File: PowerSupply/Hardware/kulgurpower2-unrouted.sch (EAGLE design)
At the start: 182 parts, among them M1 MST2V, M2 MST2V, M3 MST2V, M4 MST2V, Q1 BSH103, Q2 BSH103, Q3 BSH103, Q4 BSH103, X1 1727036, X2 2534-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

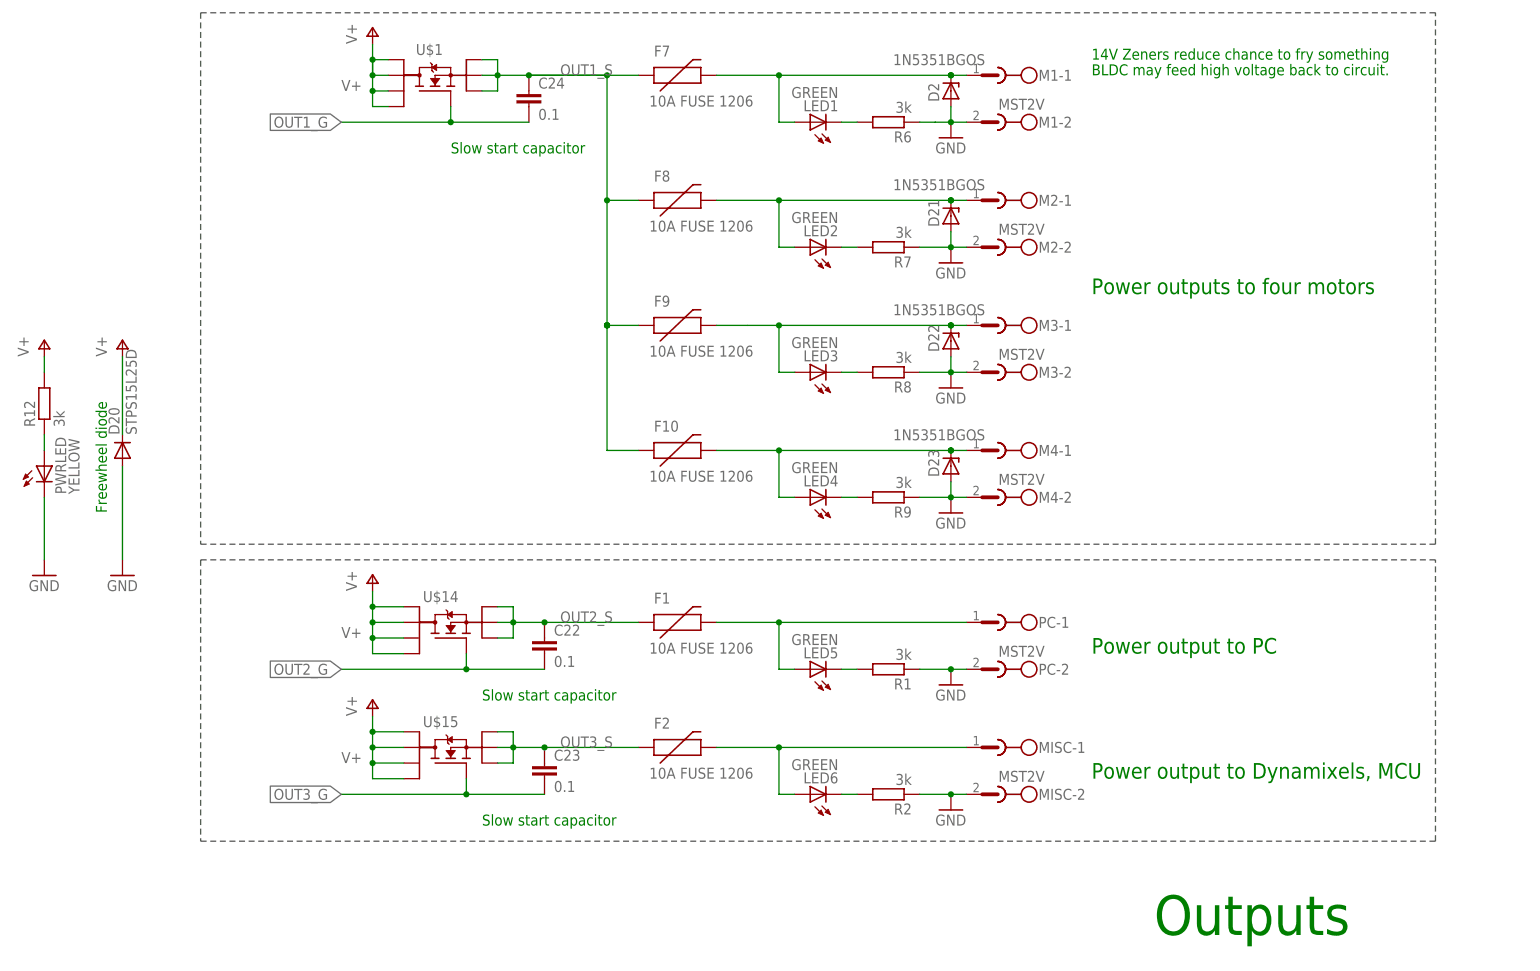
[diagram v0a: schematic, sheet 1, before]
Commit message: Schematic component type fixes
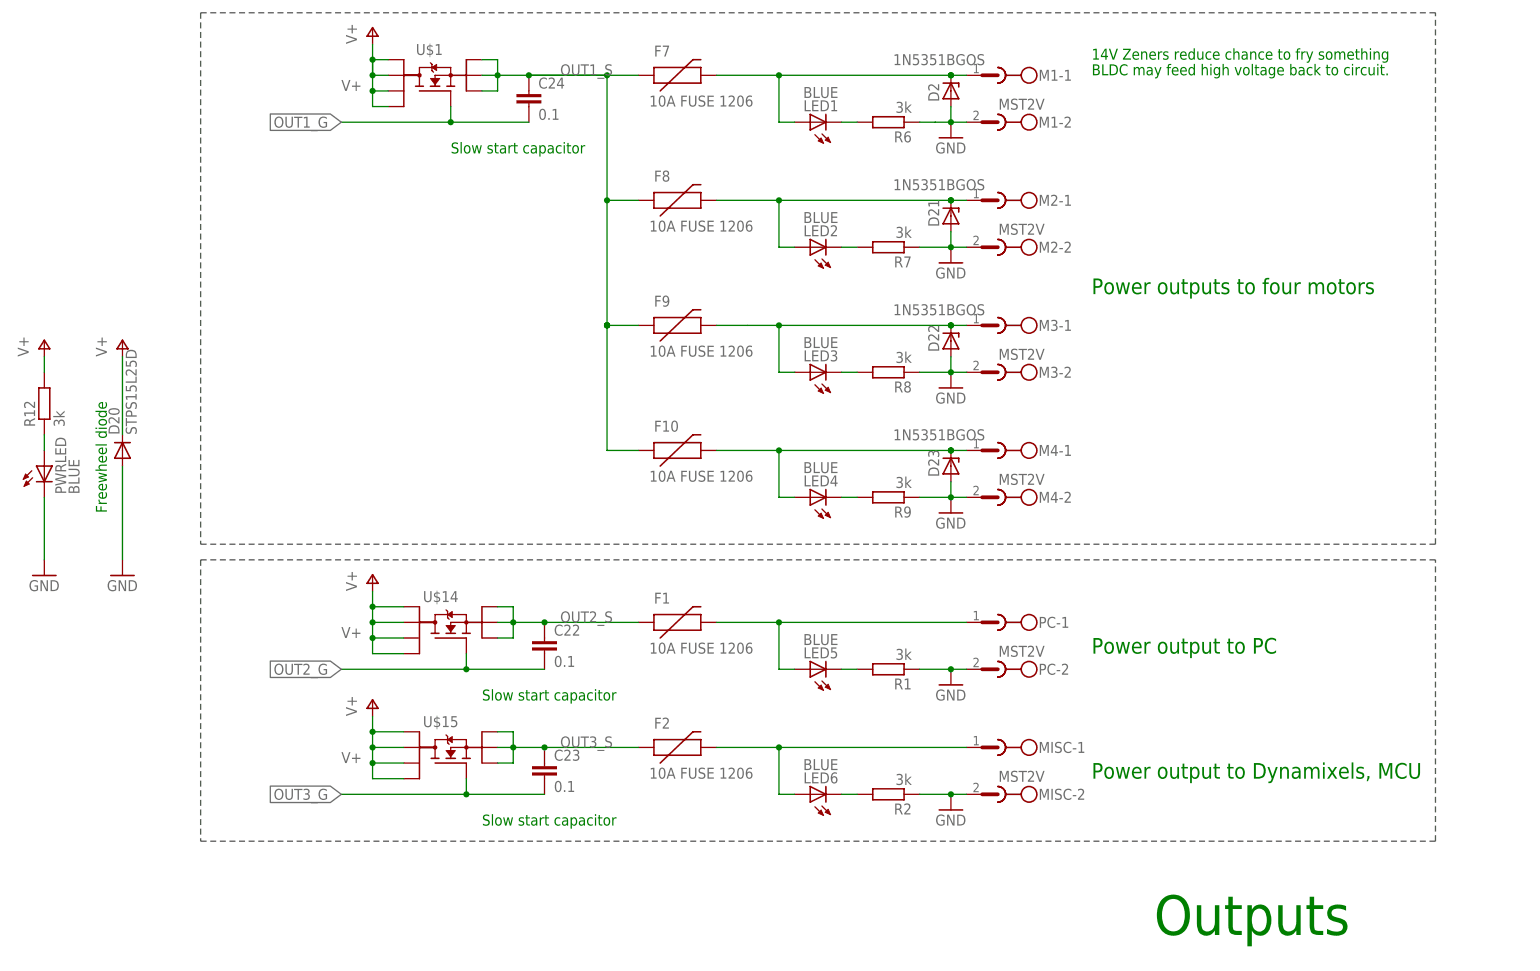
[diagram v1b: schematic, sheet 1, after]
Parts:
- LED1, LED2, LED3, LED4, LED5, LED6: value GREEN -> BLUE
- PWRLED: value YELLOW -> BLUE
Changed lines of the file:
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@@
 <part name="M4" library="con-phoenix-508" deviceset="MST2V" device=""/>
 <part name="P+2" library="supply1" deviceset="V+" device=""/>
-<part name="LED1" library="led" deviceset="LED" device="CHIP-LED0603" value="GREEN"/>
-<part name="LED2" library="led" deviceset="LED" device="CHIP-LED0603" value="GREEN"/>
-<part name="LED3" library="led" deviceset="LED" device="CHIP-LED0603" value="GREEN"/>
-<part name="LED4" library="led" deviceset="LED" device="CHIP-LED0603" value="GREEN"/>
-<part name="PWRLED" library="led" deviceset="LED" device="CHIP-LED0603" value="YELLOW"/>
+<part name="LED1" library="led" deviceset="LED" device="CHIP-LED0603" value="BLUE"/>
+<part name="LED2" library="led" deviceset="LED" device="CHIP-LED0603" value="BLUE"/>
+<part name="LED3" library="led" deviceset="LED" device="CHIP-LED0603" value="BLUE"/>
+<part name="LED4" library="led" deviceset="LED" device="CHIP-LED0603" value="BLUE"/>
+<part name="PWRLED" library="led" deviceset="LED" device="CHIP-LED0603" value="BLUE"/>
 <part name="R12" library="rcl" deviceset="R-EU_" device="R0603" value="3k"/>
 <part name="P+3" library="supply1" deviceset="V+" device=""/>
@@
 <part name="F1" library="SparkFun-PowerIC" deviceset="PTC" device="SMD" value="10A FUSE 1206"/>
 <part name="F2" library="SparkFun-PowerIC" deviceset="PTC" device="SMD" value="10A FUSE 1206"/>
-<part name="LED5" library="led" deviceset="LED" device="CHIP-LED0603" value="GREEN"/>
+<part name="LED5" library="led" deviceset="LED" device="CHIP-LED0603" value="BLUE"/>
 <part name="R1" library="rcl" deviceset="R-EU_" device="R0603" value="3k"/>
-<part name="LED6" library="led" deviceset="LED" device="CHIP-LED0603" value="GREEN"/>
+<part name="LED6" library="led" deviceset="LED" device="CHIP-LED0603" value="BLUE"/>
 <part name="R2" library="rcl" deviceset="R-EU_" device="R0603" value="3k"/>
 <part name="GND3" library="supply1" deviceset="GND" device=""/>

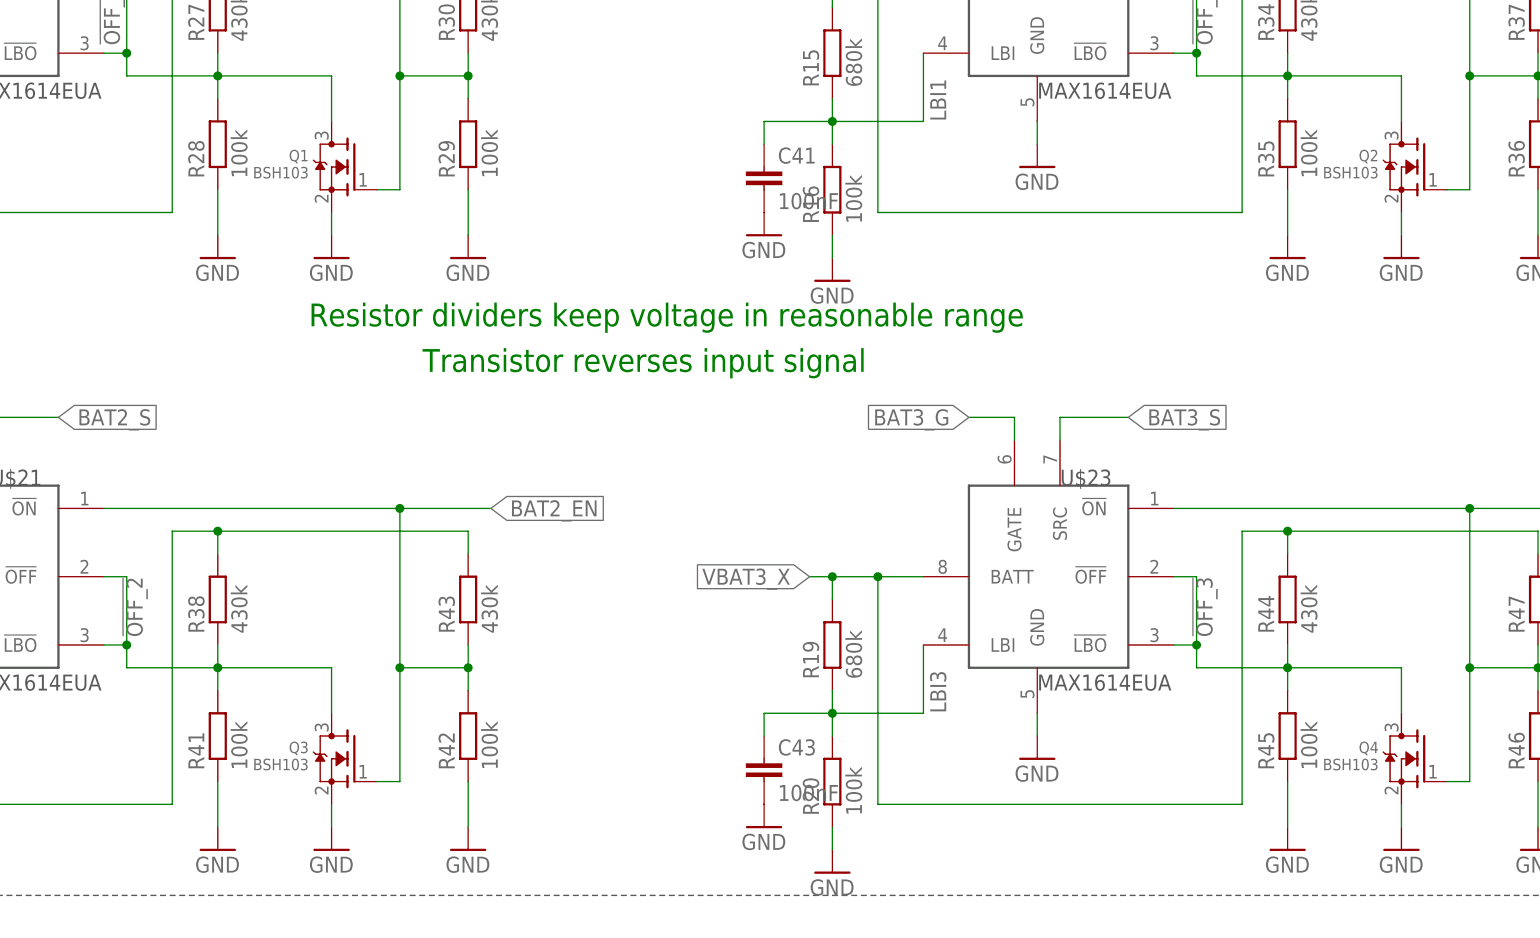
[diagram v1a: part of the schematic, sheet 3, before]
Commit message: Some values changed in schematic
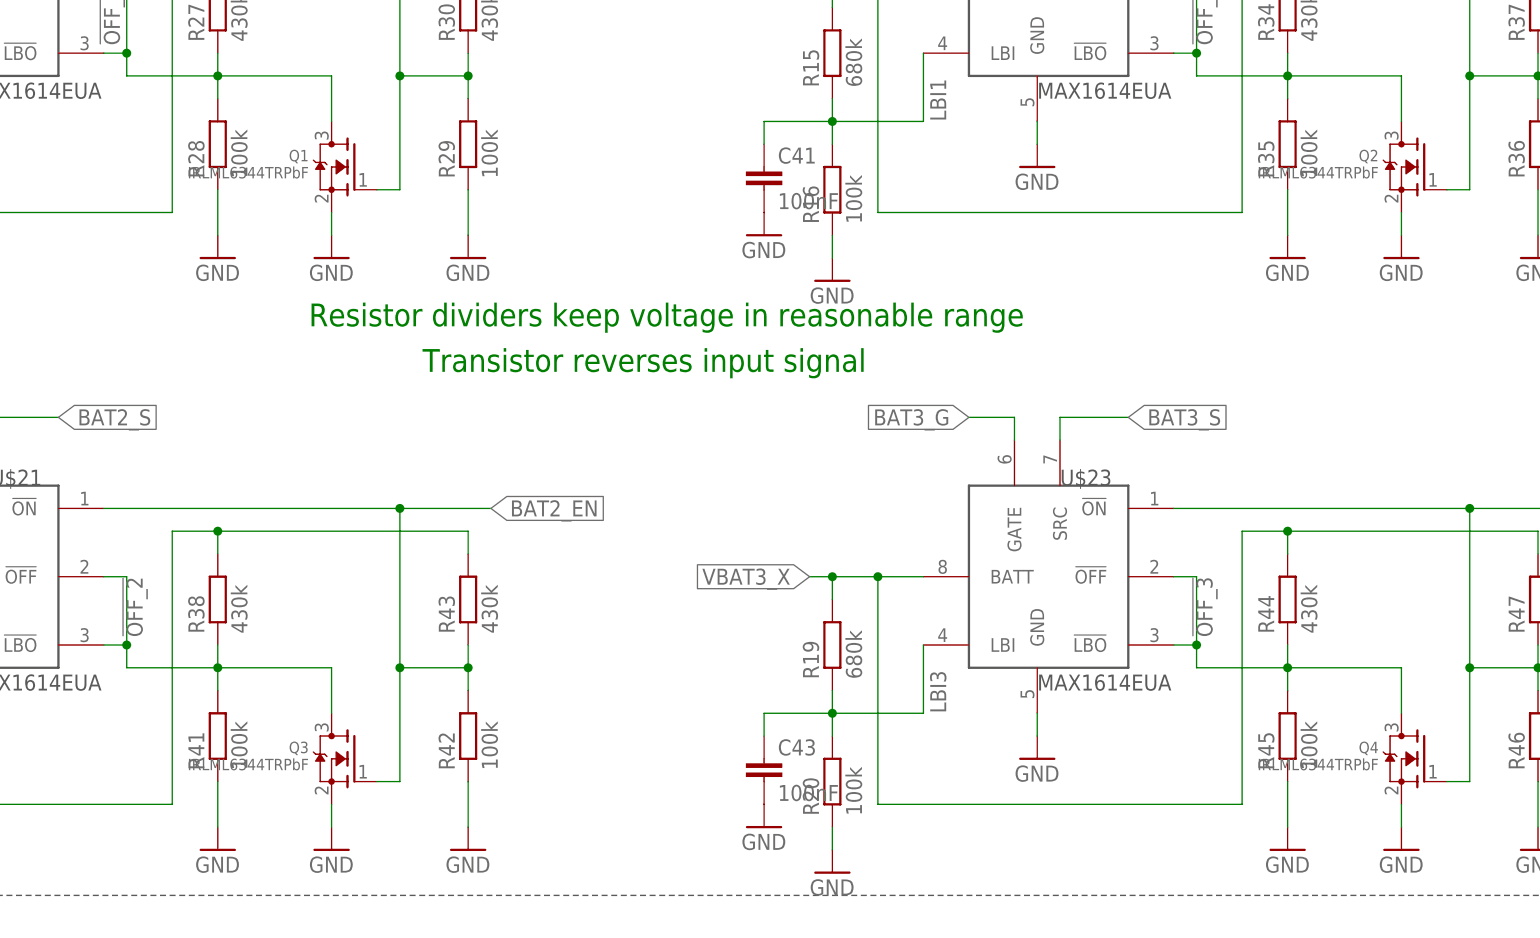
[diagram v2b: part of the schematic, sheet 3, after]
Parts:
- Q1, Q2, Q3, Q4: value BSH103 -> IRLML6344TRPbF
- R3: value 300k -> 270k
- R31, R32: value 3k16 -> 3k12
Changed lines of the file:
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@@
 <part name="GND19" library="SparkFun" deviceset="GND" device="" value="GND"/>
 <part name="GND22" library="SparkFun" deviceset="GND" device="" value="GND"/>
-<part name="R3" library="rcl" deviceset="R-EU_" device="R0603" value="300k"/>
+<part name="R3" library="rcl" deviceset="R-EU_" device="R0603" value="270k"/>
 <part name="R39" library="rcl" deviceset="R-EU_" device="R0603" value="30k"/>
 <part name="R23" library="rcl" deviceset="R-EU_" device="R0603" value="18k"/>
@@
 <part name="GND50" library="SparkFun" deviceset="GND" device=""/>
 <part name="SJ104" library="rcl" deviceset="R-EU_" device="R0603" value="0R"/>
-<part name="R31" library="rcl" deviceset="R-EU_" device="R0603" value="3k16"/>
-<part name="R32" library="rcl" deviceset="R-EU_" device="R0603" value="3k16"/>
+<part name="R31" library="rcl" deviceset="R-EU_" device="R0603" value="3k12"/>
+<part name="R32" library="rcl" deviceset="R-EU_" device="R0603" value="3k12"/>
 <part name="R25" library="rcl" deviceset="R-EU_" device="R0603" value="100k"/>
 <part name="C16" library="rcl" deviceset="C-EU" device="C0603" value="0,1u"/>
@@
 <part name="GND60" library="supply1" deviceset="GND" device=""/>
 <part name="GND62" library="supply1" deviceset="GND" device=""/>
-<part name="Q1" library="adafruit" deviceset="MOSFET-N" device="REFLOW" value="BSH103"/>
+<part name="Q1" library="adafruit" deviceset="MOSFET-N" device="REFLOW" value="IRLML6344TRPbF"/>
 <part name="GND63" library="supply1" deviceset="GND" device=""/>
 <part name="R27" library="rcl" deviceset="R-EU_" device="R0603" value="430k"/>
@@
 <part name="R30" library="rcl" deviceset="R-EU_" device="R0603" value="430k"/>
 <part name="GND65" library="supply1" deviceset="GND" device=""/>
-<part name="Q2" library="adafruit" deviceset="MOSFET-N" device="REFLOW" value="BSH103"/>
+<part name="Q2" library="adafruit" deviceset="MOSFET-N" device="REFLOW" value="IRLML6344TRPbF"/>
 <part name="GND66" library="supply1" deviceset="GND" device=""/>
 <part name="R34" library="rcl" deviceset="R-EU_" device="R0603" value="430k"/>
@@
 <part name="R37" library="rcl" deviceset="R-EU_" device="R0603" value="430k"/>
 <part name="GND68" library="supply1" deviceset="GND" device=""/>
-<part name="Q3" library="adafruit" deviceset="MOSFET-N" device="REFLOW" value="BSH103"/>
+<part name="Q3" library="adafruit" deviceset="MOSFET-N" device="REFLOW" value="IRLML6344TRPbF"/>
 <part name="GND69" library="supply1" deviceset="GND" device=""/>
 <part name="R38" library="rcl" deviceset="R-EU_" device="R0603" value="430k"/>
@@
 <part name="R43" library="rcl" deviceset="R-EU_" device="R0603" value="430k"/>
 <part name="GND71" library="supply1" deviceset="GND" device=""/>
-<part name="Q4" library="adafruit" deviceset="MOSFET-N" device="REFLOW" value="BSH103"/>
+<part name="Q4" library="adafruit" deviceset="MOSFET-N" device="REFLOW" value="IRLML6344TRPbF"/>
 <part name="GND72" library="supply1" deviceset="GND" device=""/>
 <part name="R44" library="rcl" deviceset="R-EU_" device="R0603" value="430k"/>
